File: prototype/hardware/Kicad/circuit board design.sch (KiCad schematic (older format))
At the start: 0 parts

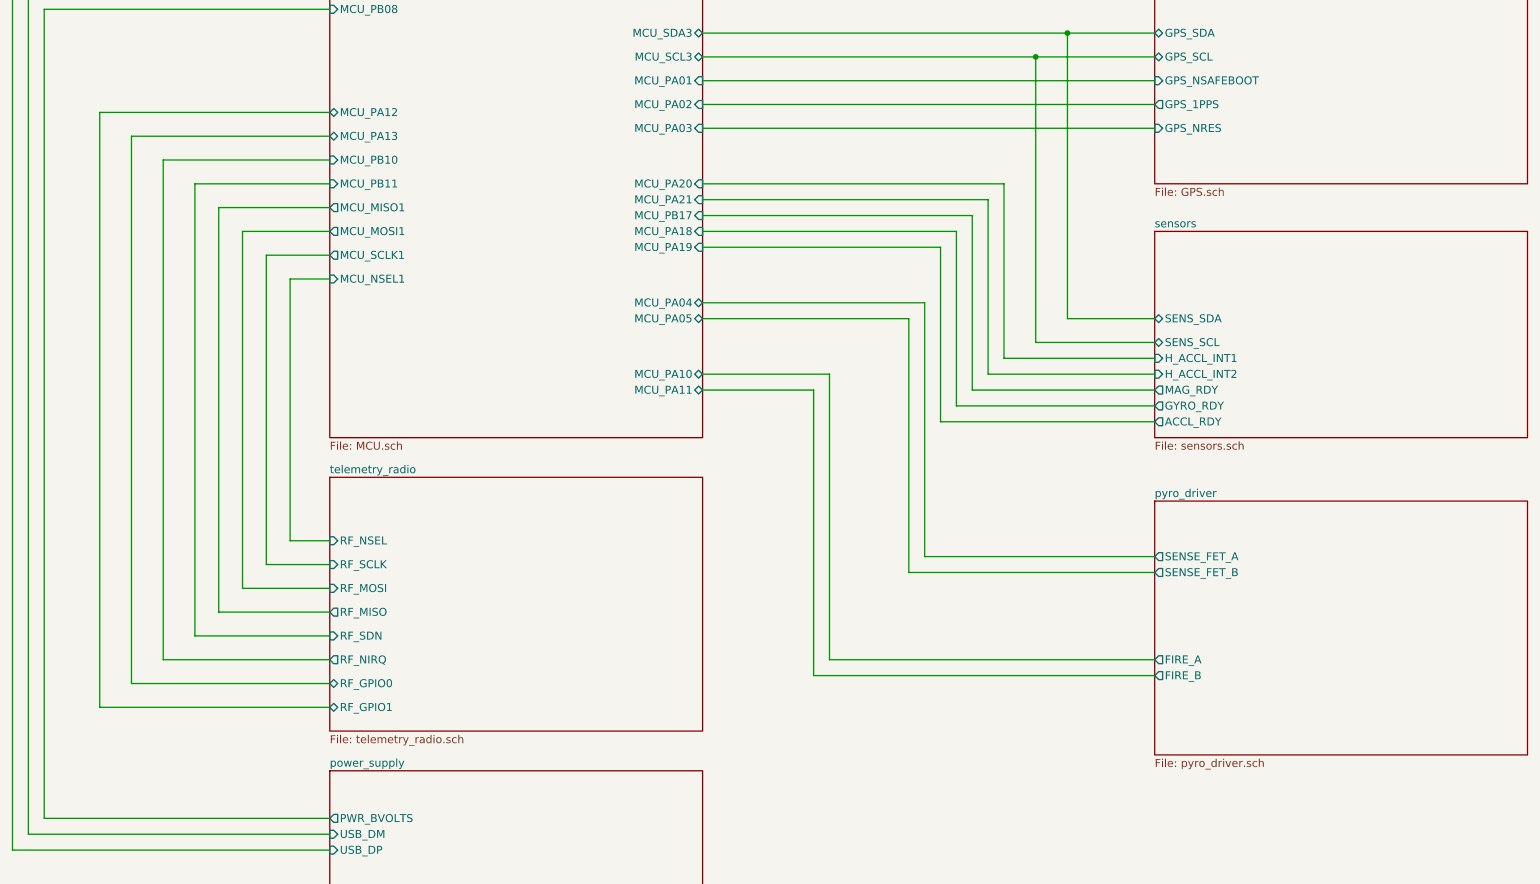
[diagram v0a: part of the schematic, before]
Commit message: removed the samd21 and put in the murata
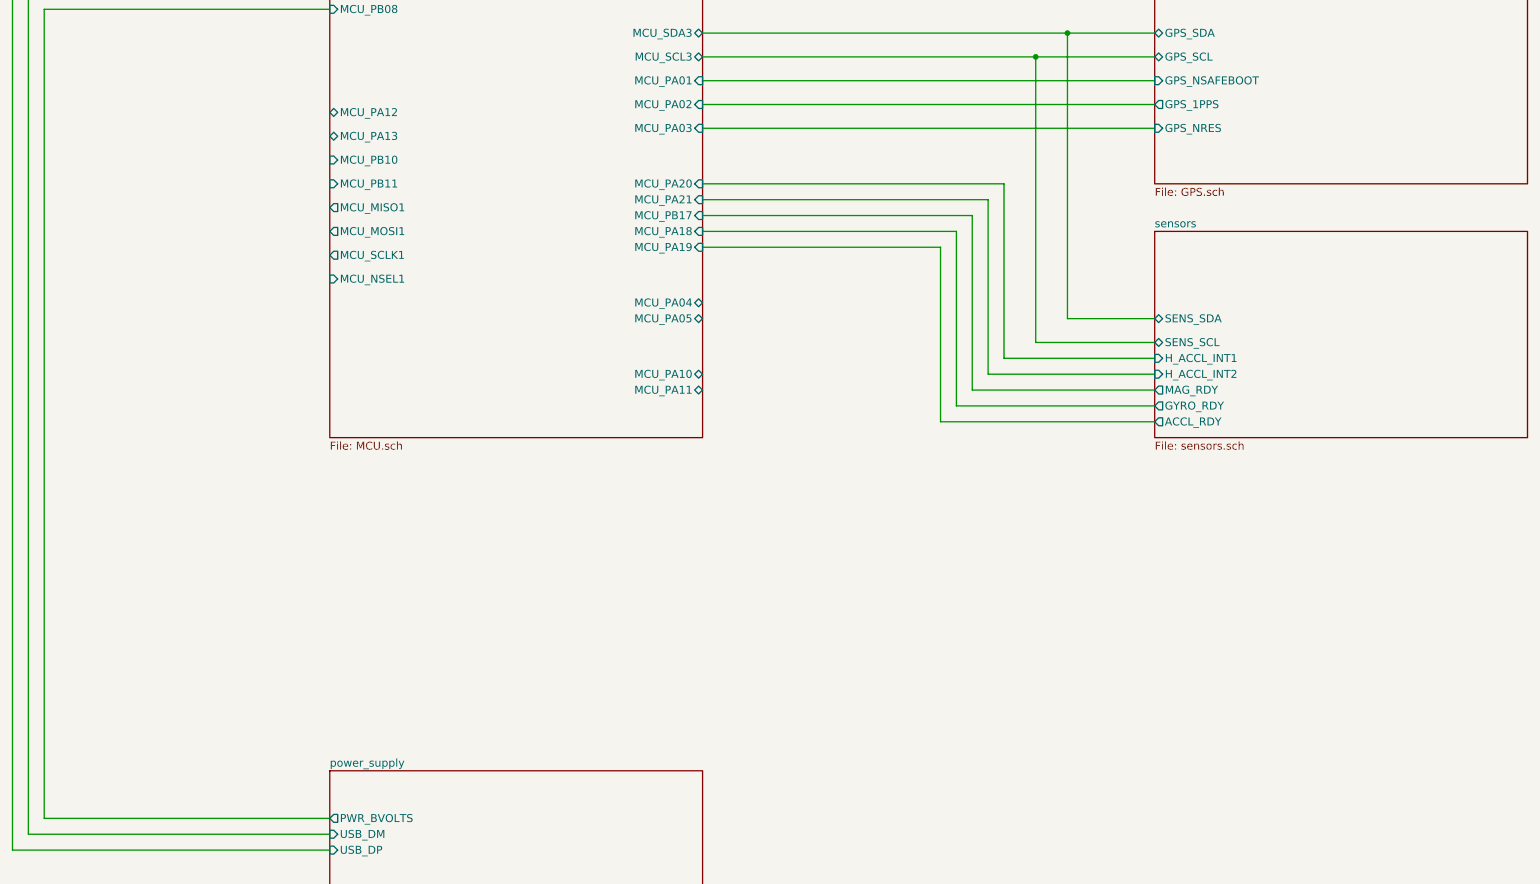
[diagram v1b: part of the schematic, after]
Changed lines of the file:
@@
 $Descr A4 11693 8268
 encoding utf-8
-Sheet 1 7
-Title "flight computer for rocket"
-Date "2019-09-09"
+Sheet 1 5
+Title "Pico lora tracker"
+Date "2019-10-19"
 Rev "1.0"
 Comp "Imperial College Space Society"
-Comment1 "Based on the Picotracker MK II"
+Comment1 "Based on the Picotracker MK II and Project mach one flight computer"
 Comment2 ""
 Comment3 ""
@@
 	7150 1900 7900 1900
 Wire Wire Line
-	2700 5700 1650 5700
-Wire Wire Line
-	2700 5550 1850 5550
-Wire Wire Line
-	2450 4950 2700 4950
-Wire Wire Line
-	2700 5250 2150 5250
-Wire Wire Line
-	2700 5400 2000 5400
-Wire Wire Line
-	2700 5100 2300 5100
-$Sheet
-S 2700 4550 2350 1600
-U 5D5B17D8
-F0 "telemetry_radio" 50
-F1 "telemetry_radio.sch" 50
-F2 "RF_SCLK" I L 2700 5100 50
-F3 "RF_MISO" O L 2700 5400 50
-F4 "RF_MOSI" I L 2700 5250 50
-F5 "RF_NSEL" I L 2700 4950 50
-F6 "RF_SDN" I L 2700 5550 50
-F7 "RF_NIRQ" O L 2700 5700 50
-F8 "RF_GPIO0" B L 2700 5850 50
-F9 "RF_GPIO1" B L 2700 6000 50
-$EndSheet
-Wire Wire Line
-	6450 3450 6450 5050
-Wire Wire Line
-	6450 5050 7900 5050
-Wire Wire Line
-	7900 5150 6350 5150
-Wire Wire Line
-	6350 5150 6350 3550
-Wire Wire Line
-	2700 5850 1450 5850
-Wire Wire Line
-	2700 6000 1250 6000
-Wire Wire Line
-	5750 4000 5050 4000
-Wire Wire Line
-	5050 3900 5850 3900
-Wire Wire Line
-	6350 3550 5050 3550
-Wire Wire Line
-	5050 3450 6450 3450
-Wire Wire Line
 	5050 1450 7900 1450
 Wire Wire Line
@@
 Wire Wire Line
 	5050 1750 7350 1750
-Wire Wire Line
-	1850 2700 1850 5550
-Wire Wire Line
-	2450 3300 2450 4950
-Wire Wire Line
-	1650 2550 2700 2550
-Wire Wire Line
-	1450 2400 2700 2400
-Wire Wire Line
-	1850 2700 2700 2700
-Wire Wire Line
-	2150 3000 2700 3000
-Wire Wire Line
-	2300 3150 2700 3150
-Wire Wire Line
-	2700 3300 2450 3300
-Wire Wire Line
-	1250 2250 2700 2250
-Wire Wire Line
-	1250 6000 1250 2250
-Wire Wire Line
-	1450 5850 1450 2400
-Wire Wire Line
-	1650 5700 1650 2550
-Wire Wire Line
-	2150 5250 2150 3000
-Wire Wire Line
-	2300 5100 2300 3150
 Wire Wire Line
 	2700 6700 900  6700
@@
 	700  6900 2700 6900
 Wire Wire Line
-	5750 5800 5750 4000
-Wire Wire Line
-	7900 5800 5750 5800
-Wire Wire Line
-	5850 5700 7900 5700
-Wire Wire Line
-	5850 3900 5850 5700
-Wire Wire Line
 	6750 4000 7900 4000
 Wire Wire Line
@@
 	5050 1300 7900 1300
 Wire Wire Line
-	2000 2850 2700 2850
-Wire Wire Line
-	2000 2850 2000 5400
-Wire Wire Line
 	5050 2050 7900 2050
 Wire Wire Line
@@
 Wire Wire Line
 	5050 2350 7900 2350
-$Sheet
-S 7900 4700 2350 1600
-U 5D6468D5
-F0 "pyro_driver" 50
-F1 "pyro_driver.sch" 50
-F2 "SENSE_FET_A" O L 7900 5050 50
-F3 "FIRE_A" O L 7900 5700 50
-F4 "SENSE_FET_B" O L 7900 5150 50
-F5 "FIRE_B" O L 7900 5800 50
-$EndSheet
 Wire Wire Line
 	6950 3800 6950 2700

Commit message: Moved all schematic parts  to a single sheet
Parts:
- added C1, C3, C5: 0.1uF 0402, symbol Device:C_Small
- added C10, C2: 10uF 0603, symbol Device:C_Small
- added C11, C9: NF 0603, symbol Device:C_Small
- added C12: 100nF, Capacitor_SMD:C_0603_1608Metric, symbol Device:C_Small
- added C13: 10uF, Capacitor_SMD:C_0603_1608Metric, symbol Device:C_Small
- added C14: 220nF, Capacitor_SMD:C_0603_1608Metric, symbol Device:C_Small
- added C15: 10nF, Capacitor_SMD:C_0402_1005Metric, symbol Device:C_Small
- added C4, C8: 1uF, Capacitor_SMD:C_0603_1608Metric, symbol Device:C
- added C6: 10nF, Capacitor_SMD:C_0603_1608Metric, symbol Device:C
- added C7: 1uF 0603, symbol Device:C_Small
- added D1: DFLS130L, Diode_SMD:D_PowerDI-123, symbol flight-computer:DFLS130L
- added J1: Conn_01x06, symbol Connector_Generic:Conn_01x06
- added J2: USB_B_Micro, flight-computer:USB_Micro-B_Molex-105017-0001, symbol Connector:USB_B_Micro
- added J3: Conn_01x02, Connector_JST:JST_PH_B2B-PH-K_1x02_P2.00mm_Vertical, symbol Connector_Generic:Conn_01x02
- added J4: Conn_Coaxial, symbol Connector:Conn_Coaxial
- added J5: Conn_Coaxial, Connector_Coaxial:U.FL_Hirose_U.FL-R-SMT-1_Vertical, symbol Connector:Conn_Coaxial
- added L1: NF 0603, symbol Device:L
- added L2: 27nH, Resistor_SMD:R_0402_1005Metric, symbol Device:L
- added R1, R2: 120K, Resistor_SMD:R_0603_1608Metric, symbol Device:R
- added R3: 10K 0402, symbol Device:R
- added R4, R5: 4.7K, Resistor_SMD:R_0603_1608Metric, symbol Device:R
- added R6: 10 Ohm, Resistor_SMD:R_0402_1005Metric, symbol Device:R
- added U1: STF202-22T1G, Package_SO:TSOP-6_1.65x3.05mm_P0.95mm, symbol flight-computer:STF202-22T1G
- added U2: MAX40200AUK, Package_TO_SOT_SMD:SOT-23-5, symbol Analog_Switch:MAX40200AUK
- added U3: CMWX1ZZABZ-078, RF_Module:CMWX1ZZABZ, symbol RF_Module:CMWX1ZZABZ-078
- added U4: LD3985M33R_TSOT23, Package_TO_SOT_SMD:TSOT-23-5, symbol Regulator_Linear:LD3985G33R_TSOT23
- added U5: MAX-M8Q, RF_GPS:ublox_MAX, symbol RF_GPS:MAX-M8Q
- added U6: MS5607-02BA, Package_LGA:LGA-8_3x5mm_P1.25mm, symbol Sensor_Pressure:MS5607-02BA
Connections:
- new net: C9.1, L1.2, U3.26 (ANT)
- new net: R3.1, U3.43 (BOOT0)
- new net: C11.1, J4.1 (In), L1.1
- new net: J5.1 (In), L2.2, U5.11 (RF_IN)
- new net: C15.1, L2.1, R6.1
- new net: R6.2, U5.14 (VCC_RF)
- new net: C4.1, D1.1 (K), U2.5 (OUT), U4.1 (VIN), U4.3 (INH)
- new net: C6.1, U4.4 (BYP)
- new net: J2.2 (D-), U1.5 (D(OUT))
- new net: J2.3 (D+), U1.4 (D(OUT))
- new net +3V3: C10.1, C12.1, C13.1, C14.1, C2.1, C3.1, C5.1, C7.1, C8.1, J1.1 (Pin_1), R4.1, R5.1, U3.4 (VDD_USB), U3.5 (VDD_MCU), U3.6 (VDD_RF), U4.5 (VOUT), U5.6 (V_BCKP), U5.7 (VCC_IO), U5.8 (VCC), U6.1 (VDD), U6.2 (PS)
- new net GND: C1.2, C10.2, C11.2, C12.2, C13.2, C14.2, C15.2, C2.2, C3.2, C4.2, C5.2, C6.2, C7.2, C8.2, C9.2, J1.3 (Pin_3), J2.5 (GND), J2.6 (Shield), J3.2 (Pin_2), J4.2 (Ext), J5.2 (Ext), R2.2, R3.2, U1.6 (GND), U2.2 (GND), U3.25 (GND), U3.27 (GND), U3.3 (GND), U3.44 (GND), U3.49 (GND), U3.50 (GND), U3.51 (GND), U3.52 (GND), U3.53 (GND), U3.54 (GND), U3.55 (GND), U3.56 (GND), U3.57 (GND), U3.7 (GND), U4.2 (GND), U5.1 (GND), U5.10 (GND), U5.12 (GND), U6.3 (GND), U6.4 (CSB), U6.5 (CSB)
- new net GPS_1PPS: U5.4 (TIMEPULSE)
- new net GPS_NRES: U5.9 (~RESET)
- new net GPS_NSAFEBOOT: U5.18 (~SAFEBOOT)
- new net GPS_RXD: U5.3 (RXD)
- new net GPS_SCL: U5.17 (SCL)
- new net GPS_SDA: U5.16 (SDA)
- new net GPS_TXD: U5.2 (TXD)
- new net I2C1_SCL: U3.35 (PB8/I2C1_SCL)
- new net I2C1_SDA: U3.36 (PB9/I2C1_SDA)
- new net PWR_BVOLTS: R1.2, R2.1
- new net RESET: C1.1, J1.5 (Pin_5), U3.34 (~MCU_RST)
- new net SENS_SCL: R5.2, U6.8 (SCLK)
- new net SENS_SDA: R4.2, U6.7 (SDI/SDA)
- new net SWCLK: J1.2 (Pin_2), U3.42 (PA14/SWCLK)
- new net SWDIO: J1.4 (Pin_4), U3.41 (PA13/SWDIO)
- new net USB_DM: U1.2 (D(IN))
- new net USB_DP: U1.3 (D(IN))
- new net VBUS: D1.2 (A), J2.1 (VBUS), U1.1 (VBUS)
- new net VDD_TCXO: U3.1 (PA12/USB_DP), U3.48 (VDD_TCXO)
- new net Vdrive: J3.1 (Pin_1), R1.1, U2.1 (VDD), U2.3 (EN)
- no-connect marks 0 -> 5
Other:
- note added: "1A Ideal Diode with Ultra-Low Voltage Drop.\n43mV drop at 500mA draw"
- note added: "3.6V-4.2V Li-po input. Needs to be\nregulated down to 3.3V cmos"
- note added: "Connected to active antenna, likely 2066400001 \nMolex active antenna. UFL connector\n"
- note added: "Debugging and programming\ninterface"
- note added: "Layout according to MAX-8 / MAX-M8, \nHardware Integration Manual,\nSection 2.4.2 Antenna design with active antenna."
- note added: "May have to increase \nthe smoothing caps to 10uF \nfor stronger effect."
- note added: "The maximum possible voltage drop(from 3.6V input) due to diode \nand LDO regulator is 173mV, leaving plenty of \nleeway to bring it down to 3.3V CMOS level."
- note added: "Ultra low drop out voltage regulator.\n140mV drop at max current of 150mA."
- note added: "http://www.explorelabs.com/blog/designing-a-gps-receiver/#ref-ublox-datasheet\n\nImportant info on why we use the components\n"

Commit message: wired up GPS
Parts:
- removed C15: 10nF, Capacitor_SMD:C_0402_1005Metric, symbol Device:C_Small
- removed C4, C8: 1uF, Capacitor_SMD:C_0603_1608Metric, symbol Device:C
- removed C6: 10nF, Capacitor_SMD:C_0603_1608Metric, symbol Device:C
- removed D1: DFLS130L, Diode_SMD:D_PowerDI-123, symbol flight-computer:DFLS130L
- removed J2: USB_B_Micro, flight-computer:USB_Micro-B_Molex-105017-0001, symbol Connector:USB_B_Micro
- removed J3: Conn_01x02, Connector_JST:JST_PH_B2B-PH-K_1x02_P2.00mm_Vertical, symbol Connector_Generic:Conn_01x02
- removed J4: Conn_Coaxial, symbol Connector:Conn_Coaxial
- removed J5: Conn_Coaxial, Connector_Coaxial:U.FL_Hirose_U.FL-R-SMT-1_Vertical, symbol Connector:Conn_Coaxial
- removed L2: 27nH, Resistor_SMD:R_0402_1005Metric, symbol Device:L
- removed R1, R2: 120K, Resistor_SMD:R_0603_1608Metric, symbol Device:R
- removed R6: 10 Ohm, Resistor_SMD:R_0402_1005Metric, symbol Device:R
- removed U1: STF202-22T1G, Package_SO:TSOP-6_1.65x3.05mm_P0.95mm, symbol flight-computer:STF202-22T1G
- removed U2: MAX40200AUK, Package_TO_SOT_SMD:SOT-23-5, symbol Analog_Switch:MAX40200AUK
- removed U4: LD3985M33R_TSOT23, Package_TO_SOT_SMD:TSOT-23-5, symbol Regulator_Linear:LD3985G33R_TSOT23
- removed U5: MAX-M8Q, RF_GPS:ublox_MAX, symbol RF_GPS:MAX-M8Q
- added AE1: Lora Antenna, symbol Device:Antenna
- added AE2: GPS Antenna, symbol Device:Antenna
- added SC1, SC2, SC3, SC4, SC5, SC6: Solar_Cell, symbol Device:Solar_Cell
- added U1: MAX-M8C, RF_GPS:ublox_MAX, symbol RF_GPS:MAX-M8C
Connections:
- net SENS_SCL is gone; now on net I2C1_SCL: R5.2, U6.8 (SCLK)
- net SENS_SDA is gone; now on net I2C1_SDA: R4.2, U6.7 (SDI/SDA)
- net +3V3: now also SC6.1 (+), U1.6 (V_BCKP), U1.7 (VCC_IO), U1.8 (VCC), U1.9 (~RESET)
- net GND: now also SC1.2 (-), U1.1 (GND), U1.10 (GND), U1.12 (GND)
- net I2C1_SCL: now also U1.17 (SCL)
- net I2C1_SDA: now also U1.16 (SDA)
- net VDD_TCXO: now also U3.15 (PB14/SPI2_MISO); no longer U3.1 (PA12/USB_DP)
- net GPS_TIMEPULSE: now reaches U3.14 (PB15/SPI2_MOSI)
- net GPS_TIMEPULSE: now also U1.4 (TIMEPULSE)
- net GPS_EXTINT: now reaches U3.16 (PB13/SPI2_SCK)
- net GPS_EXTINT: now also U1.5 (EXTINT)
- net GPS_SAFEBOOT: now reaches U3.17 (PB12/SPI2_NSS)
- net GPS_SAFEBOOT: now also U1.18 (~SAFEBOOT)
- net at C11.1, L1.1: now also AE1.1 (A)
- new net: AE2.1 (A), U1.11 (RF_IN)
- new net: SC1.1 (+), SC2.2 (-)
- new net: SC2.1 (+), SC3.2 (-)
- new net: SC3.1 (+), SC4.2 (-)
- new net: SC4.1 (+), SC5.2 (-)
- new net: SC5.1 (+), SC6.2 (-)
- no-connect marks 5 -> 30
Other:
- note added: "0.5V solar cells"
- note added: "GPS circuit\n"
- note added: "Main Microcontroller + Lora tranceiver\n"
- note added: "Ok, it is not as simple as this. -Medad 21/10/19"
- note added: "Power supply\n"
- note added: "Pressure temperature humidity sensor\n"
- note removed: "1A Ideal Diode with Ultra-Low Voltage Drop.\n43mV drop at 500mA draw"
- note removed: "3.6V-4.2V Li-po input. Needs to be\nregulated down to 3.3V cmos"
- note removed: "Connected to active antenna, likely 2066400001 \nMolex active antenna. UFL connector\n"
- note removed: "Layout according to MAX-8 / MAX-M8, \nHardware Integration Manual,\nSection 2.4.2 Antenna design with active antenna."
- note removed: "May have to increase \nthe smoothing caps to 10uF \nfor stronger effect."
- note removed: "The maximum possible voltage drop(from 3.6V input) due to diode \nand LDO regulator is 173mV, leaving plenty of \nleeway to bring it down to 3.3V CMOS level."
- note removed: "Ultra low drop out voltage regulator.\n140mV drop at max current of 150mA."
- note removed: "http://www.explorelabs.com/blog/designing-a-gps-receiver/#ref-ublox-datasheet\n\nImportant info on why we use the components\n"
- moved on the sheet: C12, C13, C14, R4, R5, U6

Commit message: updated circuit
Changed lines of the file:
@@
 Wire Wire Line
 	5350 4300 4550 4300
-Text Label 4250 4300 0    50   ~ 0
+Text Label 4000 4300 0    50   ~ 0
 RESET
 Wire Wire Line
@@
 Connection ~ 4550 4300
 Wire Wire Line
-	4550 4300 4250 4300
+	4550 4300 4000 4300
 $Comp
 L power:GND #PWR?
